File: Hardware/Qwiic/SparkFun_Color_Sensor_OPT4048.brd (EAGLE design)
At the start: 25.4 x 25.4 mm, 39 parts, among them J1 QWIIC_RIGHT_ANGLE, J2 QWIIC_RIGHT_ANGLE, U1 OPT4048

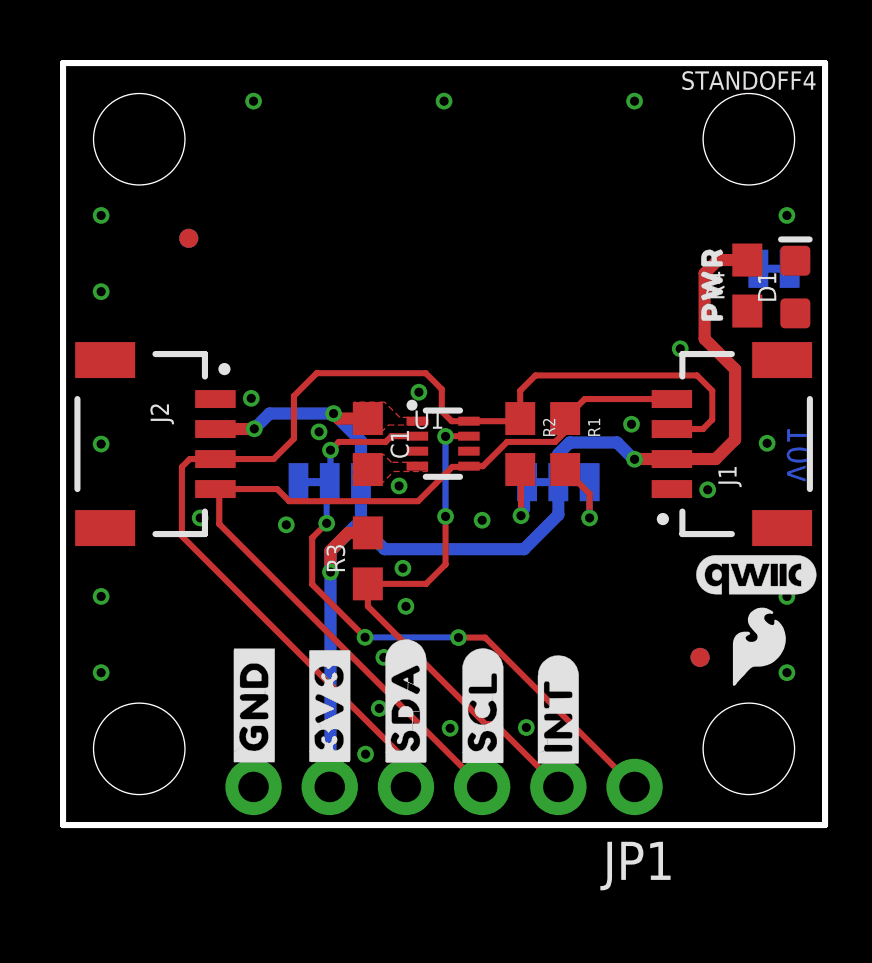
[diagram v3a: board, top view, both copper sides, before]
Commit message: Routes Qwiic board
* Adds ADDR2 jumper for SDA
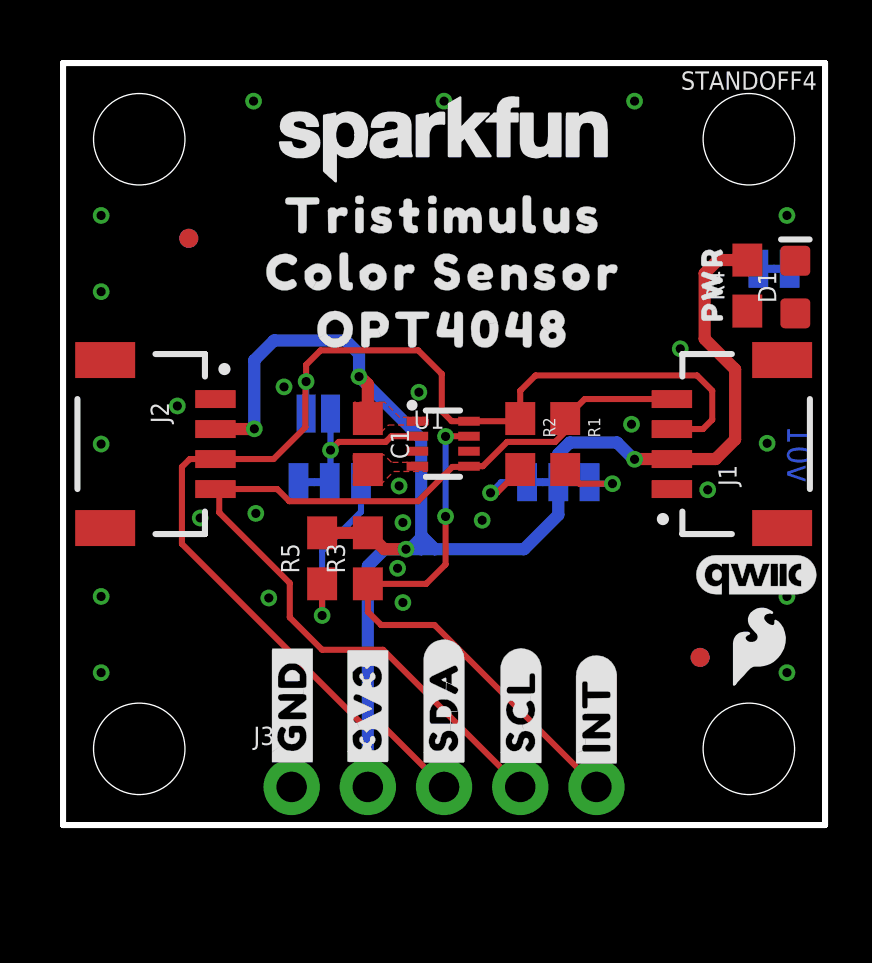
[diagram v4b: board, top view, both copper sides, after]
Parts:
- removed JP1: IO, SparkFun-Connectors:1X06_NO_SILK
- removed U$25: (no value), bot:#I2C#11
- added ADDR2: JUMPER-SMT_2_NO_SILK, SparkFun-Jumpers:SMT-JUMPER_2_NO_SILK
- added J3: (no value), SparkFun-Connectors:1X05_NO_SILK
- added R5: 10k, SparkFun-Resistors:0603
- added U$10: (no value), top:#I2C#227
- added U$11: (no value), bot:#ADDR#11
- added U$12: (no value), top:COLOR_SENSOR227
- added U$13: (no value), top:TRISTIMULUS228
- added U$14: (no value), top:OPT4048229
- added U$18: (no value), SparkFun-Aesthetics:SFE_LOGO_NAME_.1
- added U$8: (no value), bot:#ADDR2#12
- moved LOGO3 11.6 mm to (12.7, 20.6), turned to 0 degrees
- moved U$17 1.27 mm to (7.65, 3.99)
- moved U$2 1.27 mm to (7.65, 3.99)
- moved U$1 1.27 mm to (10.2, 3.96)
- moved U$15 1.27 mm to (10.2, 3.96)
- moved U$22 1.27 mm to (15.3, 3.81)
- moved U$3 1.27 mm to (12.7, 3.94)
- moved U$4 1.27 mm to (12.7, 3.96)
- moved U$5 1.27 mm to (15.3, 3.81)
- moved U$6 1.27 mm to (17.8, 3.68)
- moved U$7 1.27 mm to (17.8, 3.68)
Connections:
- new net N$1: ADDR.1, R5.1
- net 3.3V: now also J3.2, R5.2; no longer ADDR.1, JP1.5
- net ADDR: now also ADDR2.1; no longer JP1.1
- net GND: now also J3.1; no longer JP1.6
- net INT: now also J3.5; no longer JP1.2
- net SCL: now also J3.4; no longer JP1.3
- net SDA: now also ADDR2.2, J3.3; no longer JP1.4
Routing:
- net ADDR: track 21.4 -> 5.53 mm, vias 4 -> 1
- net 3.3V: track 44.5 -> 51.4 mm
- net N$1: track 0.00 -> 6.04 mm, vias 0 -> 1
- net SDA: track 38.5 -> 41.8 mm, vias 0 -> 1
- net SCL: track 30.6 -> 32.3 mm
- net INT: track 17.5 -> 18.9 mm
- net N$5: track 3.14 -> 2.55 mm

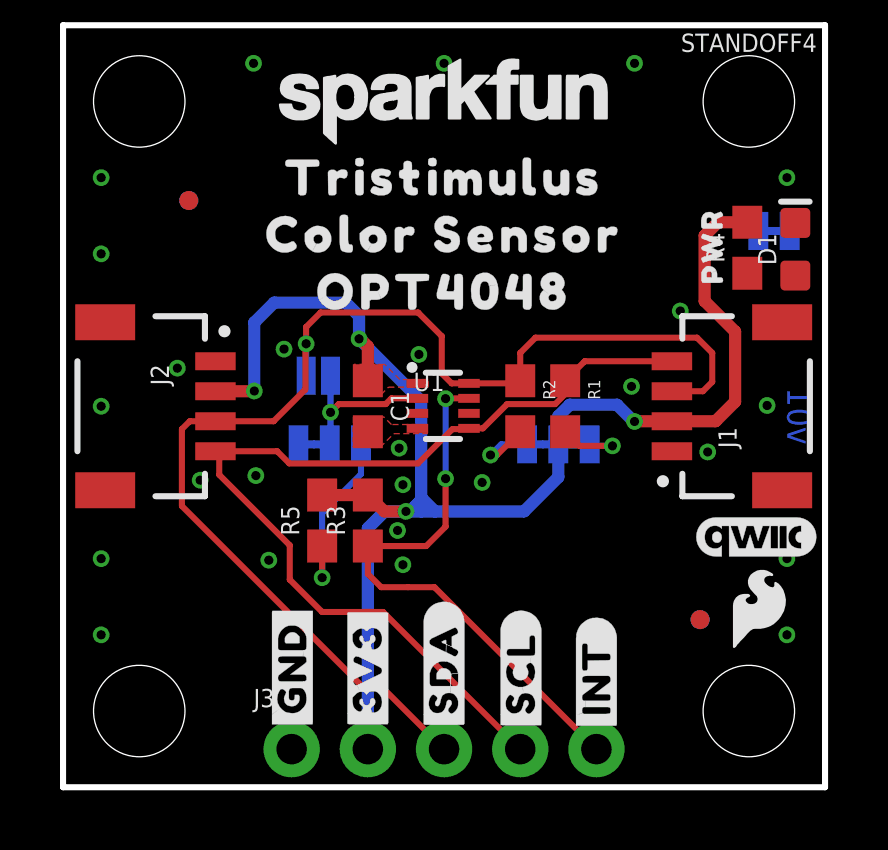
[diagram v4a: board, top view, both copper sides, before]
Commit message: Improves ground pour
* Improves schematic aesthetic
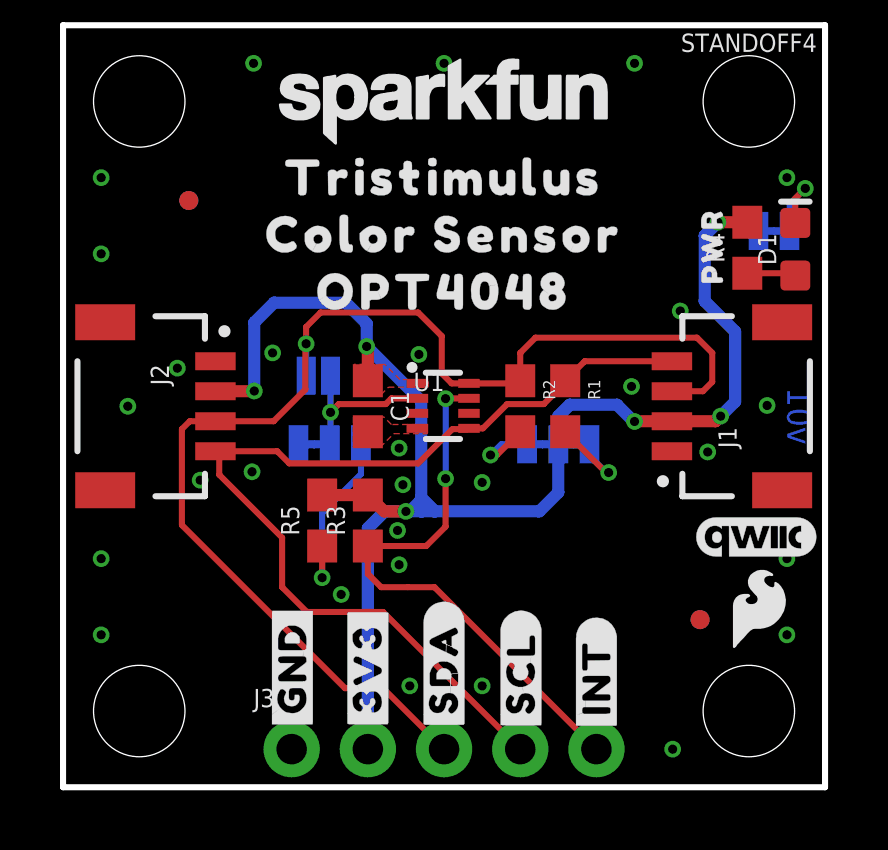
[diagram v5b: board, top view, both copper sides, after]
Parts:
- moved LOGO2 21.7 mm to (2.16, 12.7)
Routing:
- net N$3: track 0.00 -> 2.93 mm, vias 0 -> 1
- net N$2: track 0.00 -> 1.63 mm
- net N$5: track 2.55 -> 3.26 mm
- net 3.3V: track 51.4 -> 51.3 mm, vias 4 -> 6

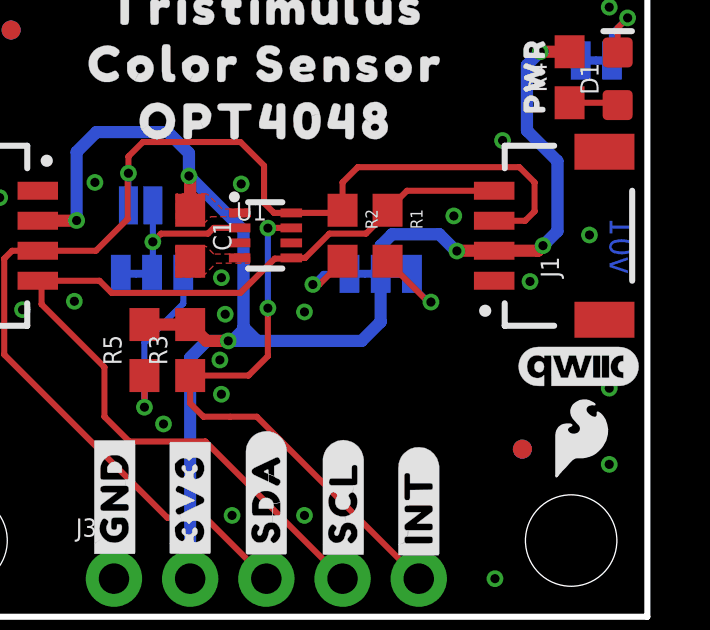
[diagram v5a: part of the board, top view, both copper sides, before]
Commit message: Finishes routing Qwiic mini
* Adds silk to Qwiic mini
* Adds ordering instructions
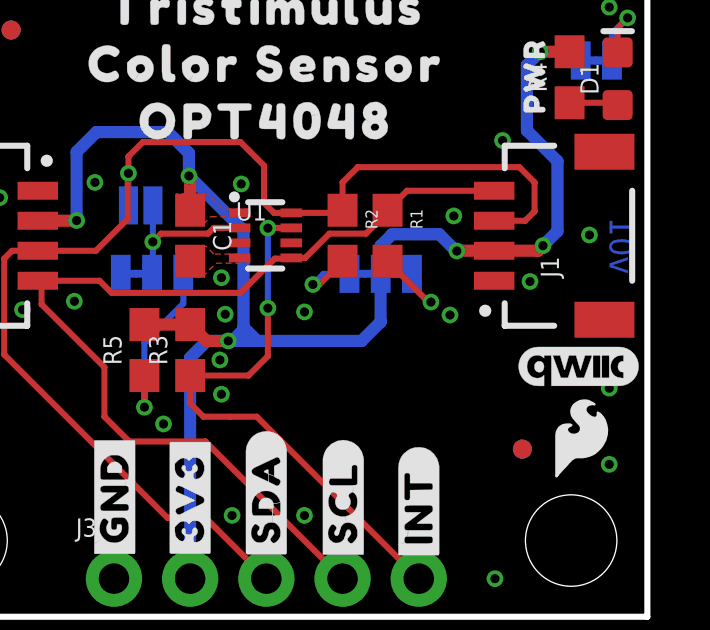
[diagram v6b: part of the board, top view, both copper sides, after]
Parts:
- added LOGO4: SPECIAL_INSTRUCTIONS-ORDERING, SparkFun-Aesthetics:ORDERING_INSTRUCTIONS
- added U$19: (no value), top:OPT4048229
- added U$20: (no value), top:DEF_ADDRESS#_17
- added U$21: (no value), top:0X4418
- added U$9: (no value), top:COLOR_SENSOR227
- moved FRAME1 8.89 mm to (-19.1, -20.3)
- moved LOGO3 0.64 mm to (12.7, 21.3)
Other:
- board text added: "1.6mm Thickness 1 oz. Copper Lead-Free HASL finish Material: TG135-140 Red Soldermask White Silkscreen"
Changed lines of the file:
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@@
 <layer number="45" name="Holes" color="7" fill="1" visible="yes" active="yes"/>
 <layer number="46" name="Milling" color="3" fill="1" visible="no" active="yes"/>
-<layer number="47" name="Measures" color="7" fill="1" visible="no" active="yes"/>
+<layer number="47" name="Measures" color="7" fill="1" visible="yes" active="yes"/>
 <layer number="48" name="Document" color="7" fill="1" visible="no" active="yes"/>
 <layer number="49" name="Reference" color="13" fill="1" visible="yes" active="yes"/>
@@
 <wire x1="25.4" y1="0" x2="25.4" y2="25.4" width="0.2032" layer="20"/>
 <text x="24.139525" y="11.420475" size="0.8128" layer="16" font="vector" ratio="22" rot="MR90">v01</text>
-<dimension x1="0" y1="25.4" x2="0" y2="0" x3="-8.636" y3="12.7" textsize="1.778" textratio="15" layer="47" unit="inch" visible="yes"/>
-<dimension x1="25.4" y1="25.4" x2="0" y2="25.4" x3="12.7" y3="30.48" textsize="1.778" textratio="15" layer="47" unit="inch" visible="yes"/>
-<dimension x1="5.08" y1="12.7" x2="5.08" y2="0" x3="-5.588" y3="6.35" textsize="1.778" textratio="15" layer="47" unit="inch" visible="yes"/>
-<dimension x1="2.54" y1="2.54" x2="2.54" y2="0" x3="-1.778" y3="1.27" textsize="1.778" textratio="15" layer="47" unit="inch"/>
-<dimension x1="2.54" y1="22.86" x2="2.54" y2="25.4" x3="-2.54" y3="24.13" textsize="1.778" textratio="15" layer="47" unit="inch" visible="yes"/>
-<dimension x1="2.54" y1="22.86" x2="22.86" y2="22.86" x3="12.7" y3="27.178" textsize="1.778" textratio="15" layer="47" unit="inch" visible="yes"/>
 <rectangle x1="12.446" y1="13.462" x2="12.4968" y2="13.7668" layer="41"/>
+<text x="31.75" y="25.4" size="1.778" layer="51" font="vector">1.6mm Thickness
+1 oz. Copper
+Lead-Free HASL finish
+Material: TG135-140
+Red Soldermask
+White Silkscreen</text>
+<dimension x1="0" y1="25.4" x2="0" y2="0" x3="-8.89" y3="12.7" textsize="1.778" layer="47" unit="inch"/>
+<dimension x1="25.4" y1="25.4" x2="0" y2="25.4" x3="12.7" y3="38.1" textsize="1.778" layer="47" unit="inch"/>
+<dimension x1="12.7" y1="12.7" x2="12.7" y2="0" x3="-5.08" y3="6.35" textsize="1.778" layer="47" unit="inch"/>
+<dimension x1="2.54" y1="2.54" x2="2.54" y2="0" x3="-1.27" y3="1.27" textsize="1.778" layer="47" unit="inch"/>
+<dimension x1="2.54" y1="22.86" x2="0" y2="22.86" x3="1.27" y3="27.94" textsize="1.778" layer="47" unit="inch"/>
+<dimension x1="12.7" y1="12.7" x2="0" y2="12.7" x3="6.35" y3="34.29" textsize="1.778" layer="47" unit="inch"/>
+<dimension x1="7.62" y1="1.27" x2="0" y2="1.27" x3="3.81" y3="-5.08" textsize="1.778" layer="47" unit="inch"/>
+<dimension x1="7.62" y1="1.27" x2="17.78" y2="1.27" x3="12.7" y3="-5.08" textsize="1.778" layer="47" unit="inch"/>
+<dimension x1="17.78" y1="1.27" x2="25.4" y2="1.27" x3="21.59" y3="-5.08" textsize="1.778" layer="47" unit="inch"/>
 </plain>
 <attributes>
@@
 </autorouter>
 <elements>
-<element name="FRAME1" library="SparkFun-Aesthetics" package="CREATIVE_COMMONS" value="FRAME-LETTER" x="-19.05" y="-11.43" smashed="yes">
-<attribute name="DESIGNER" value="Elias Santistevan" x="12.7" y="-11.43" size="1.778" layer="51" font="vector"/>
-<attribute name="REV" value="" x="-19.05" y="-11.43" size="1.778" layer="27" display="off"/>
+<element name="FRAME1" library="SparkFun-Aesthetics" package="CREATIVE_COMMONS" value="FRAME-LETTER" x="-19.05" y="-20.32" smashed="yes">
+<attribute name="DESIGNER" value="Elias Santistevan" x="12.7" y="-20.32" size="1.778" layer="51" font="vector"/>
+<attribute name="REV" value="" x="-19.05" y="-20.32" size="1.778" layer="27" display="off"/>
 </element>
 <element name="LOGO2" library="SparkFun-Aesthetics" package="OSHW-LOGO-MINI" value="OSHW-LOGOMINI" x="2.159" y="12.7" smashed="yes" rot="MR0"/>
@@
 <attribute name="VALUE" x="17.78" y="9.525" size="0.4064" layer="28" rot="MR0"/>
 </element>
-<element name="LOGO3" library="SparkFun-Aesthetics" package="SFE_LOGO_NAME_FLAME_.1" value="SFE_LOGO_NAME_FLAME.1_INCH" x="12.658725" y="20.647025" smashed="yes" rot="MR0"/>
+<element name="LOGO3" library="SparkFun-Aesthetics" package="SFE_LOGO_NAME_FLAME_.1" value="SFE_LOGO_NAME_FLAME.1_INCH" x="12.658725" y="21.282025" smashed="yes" rot="MR0"/>
 <element name="J1" library="SparkFun-Connectors" package="JST04_1MM_RA" value="QWIIC_RIGHT_ANGLE" x="20.2946" y="12.7" smashed="yes" rot="R90">
 <attribute name="NAME" x="22.4536" y="11.303" size="0.6096" layer="25" font="vector" ratio="20" rot="R90"/>
@@
 </element>
 <element name="U$8" library="bot" package="#ADDR2#12" value="" x="8.763" y="15.494" smashed="yes" rot="MR0"/>
+<element name="U$9" library="top" package="COLOR_SENSOR227" value="" x="12.7" y="19.685" smashed="yes" rot="MR0"/>
+<element name="U$19" library="top" package="OPT4048229" value="" x="12.7" y="17.78" smashed="yes" rot="MR0"/>
+<element name="U$20" library="top" package="DEF_ADDRESS#_17" value="" x="13.97" y="7.62" smashed="yes" rot="MR0"/>
+<element name="U$21" library="top" package="0X4418" value="" x="7.493" y="7.493" smashed="yes" rot="MR0"/>
+<element name="LOGO4" library="SparkFun-Aesthetics" package="ORDERING_INSTRUCTIONS" value="SPECIAL_INSTRUCTIONS-ORDERING" x="29.21" y="50.8" smashed="yes"/>
 </elements>
 <signals>
@@
 <via x="13.97" y="3.3782" extent="1-16" drill="0.3048"/>
 <via x="20.32" y="1.27" extent="1-16" drill="0.3048"/>
+<via x="18.8214" y="10.0584" extent="1-16" drill="0.3048"/>
 </signal>
 <signal name="SCL">
@@
 </drawing>
 <compatibility>
+<note version="6.3" minversion="6.2.2" severity="warning">
+Since Version 6.2.2 text objects can contain more than one line,
+which will not be processed correctly with this version.
+</note>
 <note version="8.3" severity="warning">
 Since Version 8.3, EAGLE supports URNs for individual library

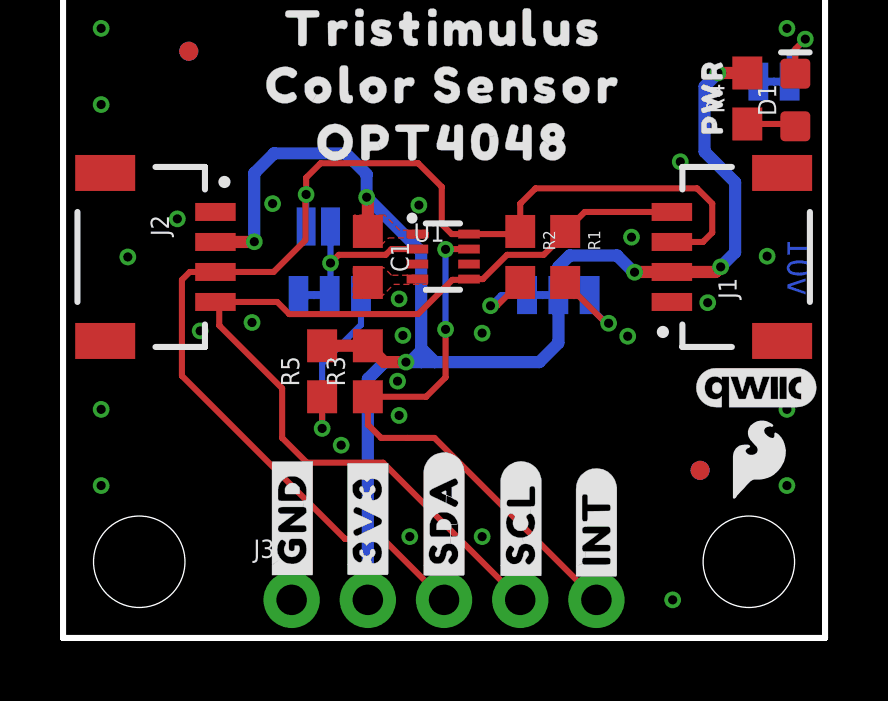
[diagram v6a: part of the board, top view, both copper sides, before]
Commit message: Changes Jumper selection, moves resistors away from IC, and changes decoupling cap to smaller package
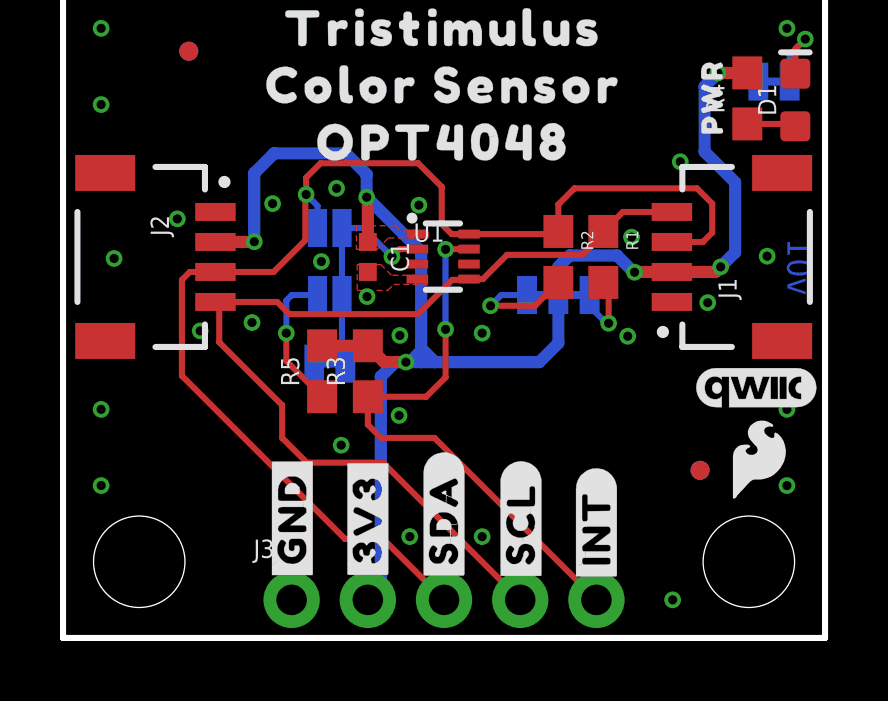
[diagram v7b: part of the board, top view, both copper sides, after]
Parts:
- removed ADDR: JUMPER-SMT_3_1-NC_TRACE_SILK, SparkFun-Jumpers:SMT-JUMPER_3_1-NC_TRACE_SILK
- removed ADDR2: JUMPER-SMT_2_NO_SILK, SparkFun-Jumpers:SMT-JUMPER_2_NO_SILK
- added 0X44: JUMPER-SMT_2_NC_TRACE_SILK, SparkFun-Jumpers:SMT-JUMPER_2_NC_TRACE_SILK
- added 0X45, 0X46: JUMPER-SMT_2_NO_SILK, SparkFun-Jumpers:SMT-JUMPER_2_NO_SILK
- C1: device SparkFun-Capacitors:0603 -> SparkFun-Capacitors:0402-TIGHT
- U$11: device bot:#ADDR#11 -> top:#0X45#18
- U$21: device top:0X4418 -> top:#0X46#18
- U$8: device bot:#ADDR2#12 -> top:#0X44#18
- moved U$8 7.15 mm to (5.54, 9.12)
- moved U$21 6.37 mm to (5.64, 13.6)
- moved U$11 3.48 mm to (5.69, 11.4)
- moved U$10 3.35 mm to (16.5, 13.1)
- moved U$20 1.93 mm to (15.0, 9.25)
- moved R2 1.27 mm to (16.5, 12.7)
- moved R1 1.27 mm to (18.0, 12.7)
- moved LOGO2 0.46 mm to (1.70, 12.6)
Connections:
- removed net N$1: ADDR.1, R5.1
- new net N$4: 0X45.2, R5.1
- net ADDR: now also 0X44.1, 0X45.1, 0X46.1; no longer ADDR.2, ADDR2.1
- net GND: now also 0X44.2; no longer ADDR.3
- net SDA: now also 0X46.2; no longer ADDR2.2
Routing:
- net N$1: track 6.04 -> 0.00 mm, vias 1 -> 0
- net N$4: track 0.00 -> 4.92 mm, vias 0 -> 1
- net ADDR: track 5.38 -> 7.97 mm
- net N$6: track 2.68 -> 3.95 mm
- net N$5: track 3.26 -> 2.68 mm
